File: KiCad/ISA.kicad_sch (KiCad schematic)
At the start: 4 parts

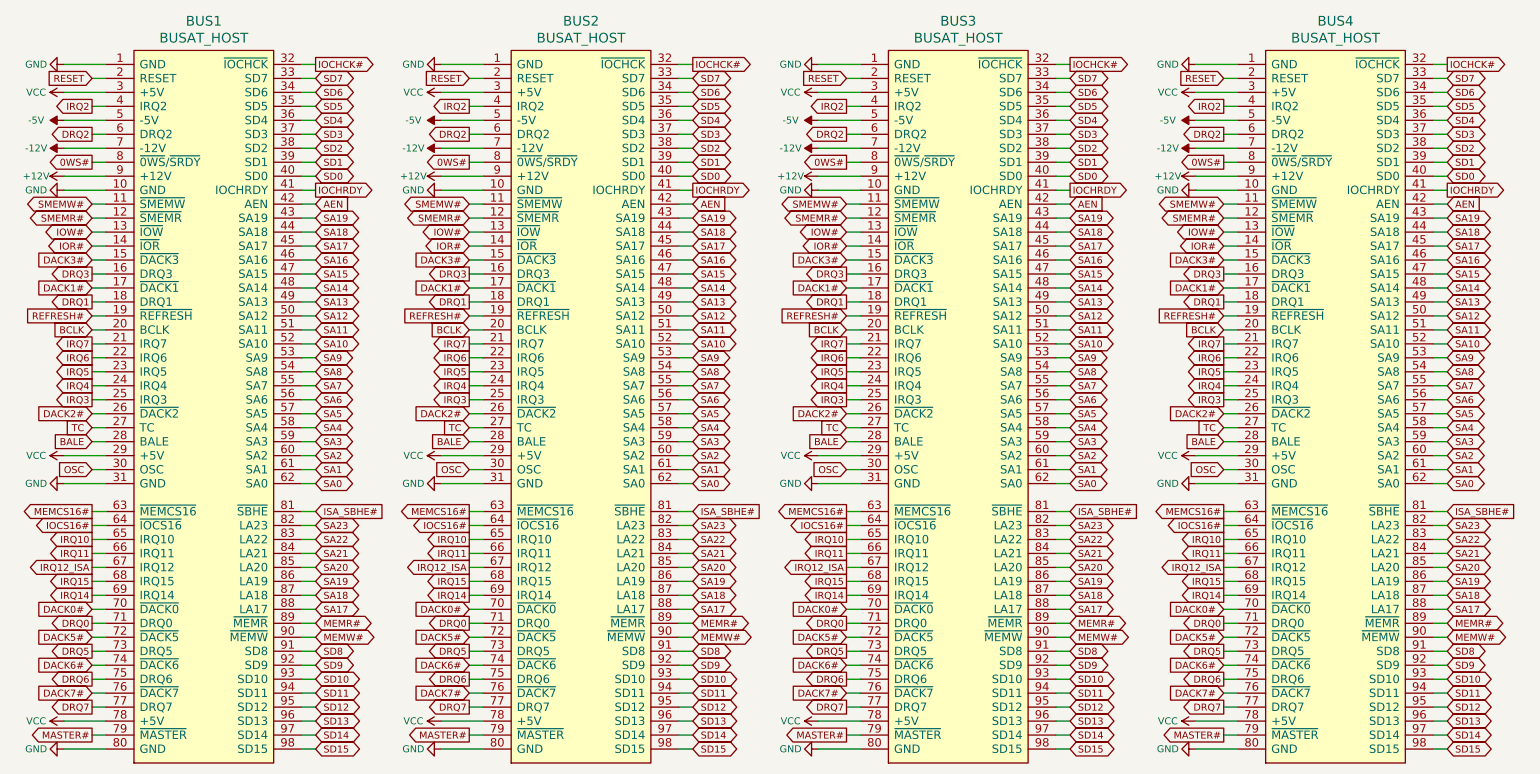
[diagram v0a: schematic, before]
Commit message: Version 0.3: Update DRAM schematic, pull-ups/pull-downs, CPU configuration jumpers
Signed-off-by: Sergey Kiselev <skiselev@gmail.com>
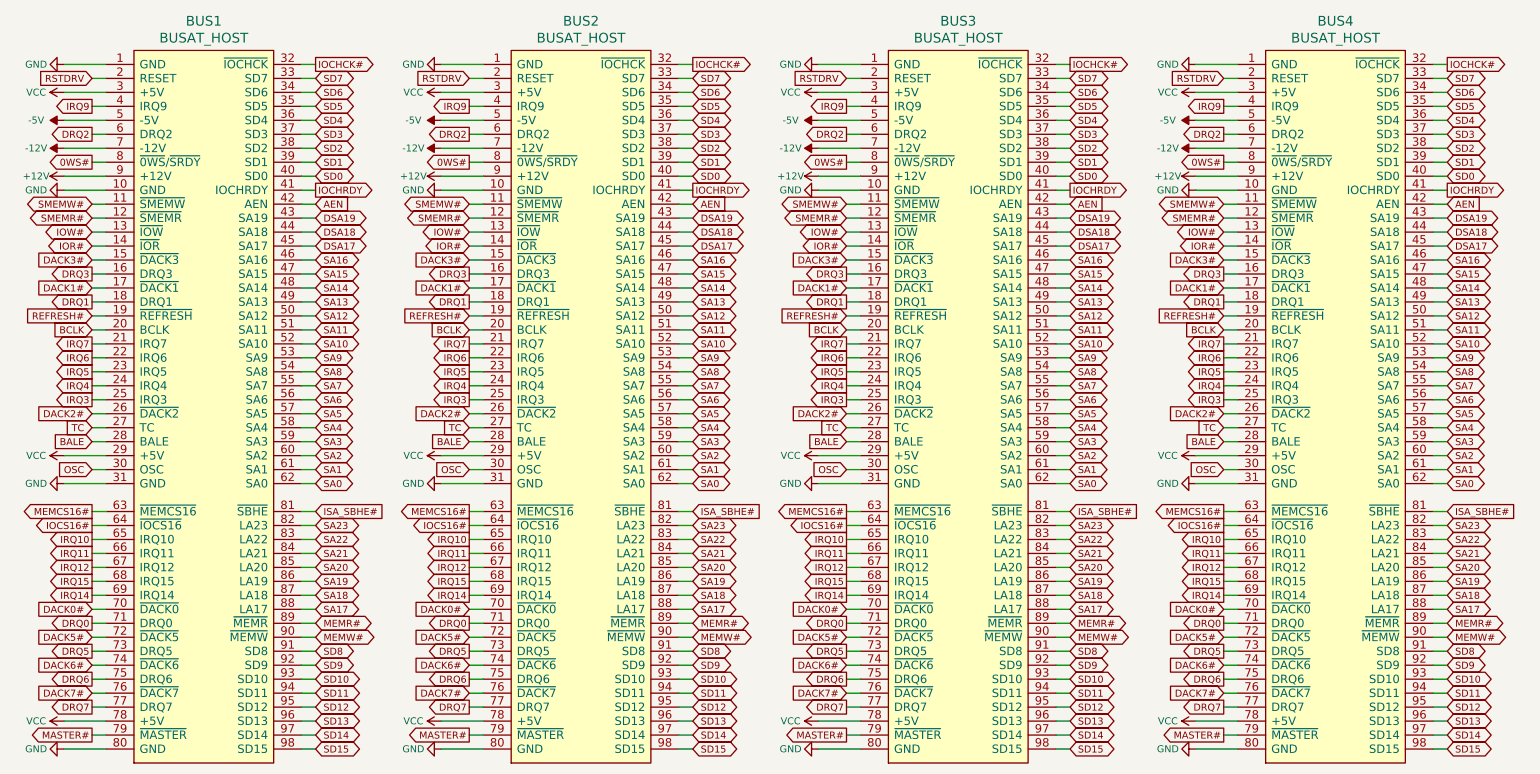
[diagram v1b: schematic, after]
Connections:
- net SA17: no longer BUS1.45 (SA17), BUS2.45 (SA17), BUS3.45 (SA17), BUS4.45 (SA17)
- net SA18: no longer BUS1.44 (SA18), BUS2.44 (SA18), BUS3.44 (SA18), BUS4.44 (SA18)
- net SA19: no longer BUS1.43 (SA19), BUS2.43 (SA19), BUS3.43 (SA19), BUS4.43 (SA19)
- net IRQ12_ISA renamed IRQ12
- net IRQ2 renamed IRQ9
- net RESET renamed RSTDRV
- new net DSA17: BUS1.45 (SA17), BUS2.45 (SA17), BUS3.45 (SA17), BUS4.45 (SA17)
- new net DSA18: BUS1.44 (SA18), BUS2.44 (SA18), BUS3.44 (SA18), BUS4.44 (SA18)
- new net DSA19: BUS1.43 (SA19), BUS2.43 (SA19), BUS3.43 (SA19), BUS4.43 (SA19)

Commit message: Version 0.4: Update chipset connection
Signed-off-by: Sergey Kiselev <skiselev@gmail.com>
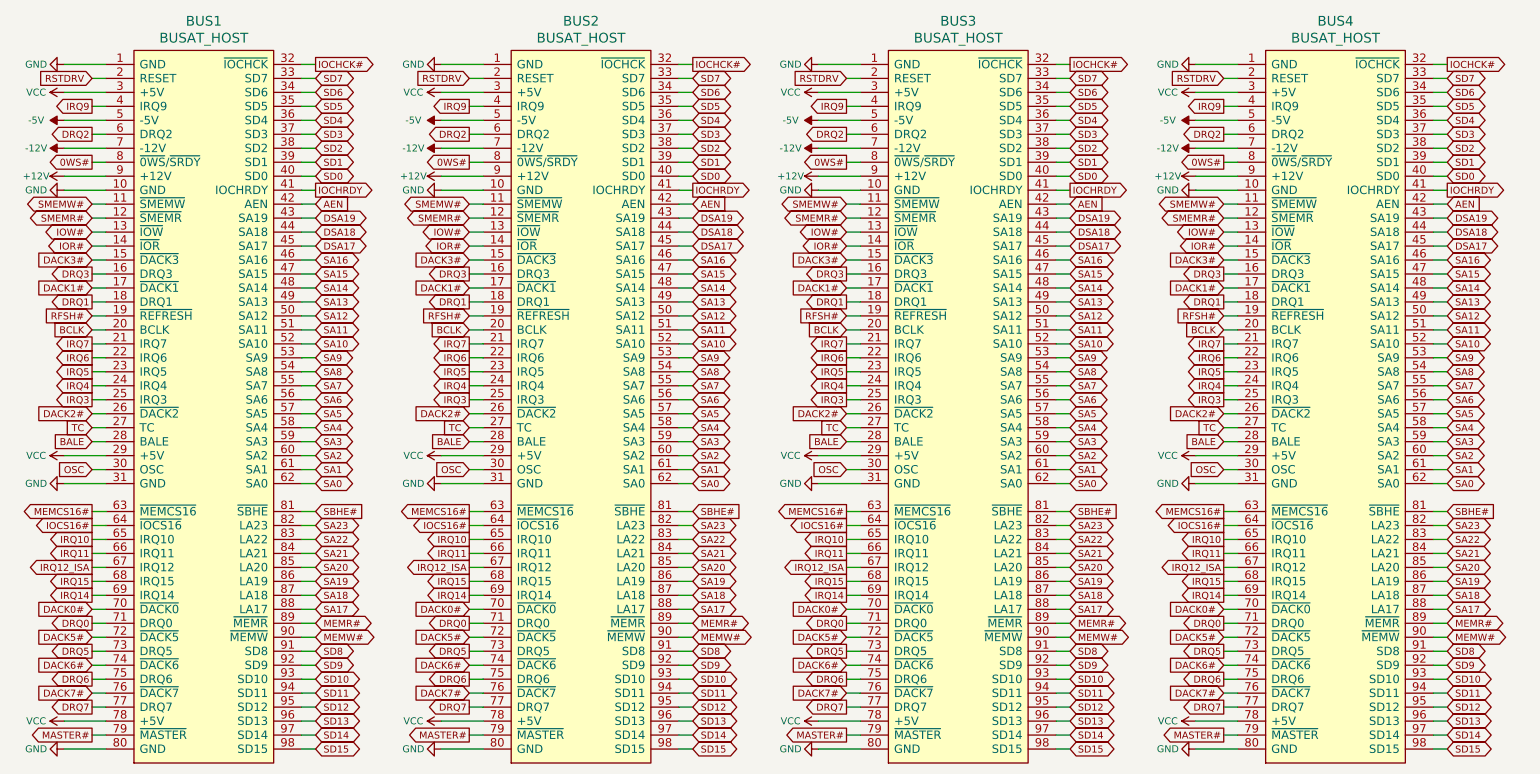
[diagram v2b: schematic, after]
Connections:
- net IRQ12 renamed IRQ12_ISA
- net ISA_SBHE# renamed SBHE#
- net REFRESH# renamed RFSH#
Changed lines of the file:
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@@
     )
   )
-  (global_label "IRQ12" (shape output) (at 231.14 116.84 180) (fields_autoplaced)
-    (effects (font (size 1.27 1.27)) (justify right))
-    (property "Intersheet References" "${INTERSHEET_REFS}" (id 0) (at 223.1915 116.7606 0)
+  (global_label "IRQ12_ISA" (shape output) (at 231.14 116.84 180) (fields_autoplaced)
+    (effects (font (size 1.27 1.27)) (justify right))
+    (property "Intersheet References" "${INTERSHEET_REFS}" (id 0) (at 219.321 116.7606 0)
       (effects (font (size 1.27 1.27)) (justify right) hide)
     )
@@
     )
   )
-  (global_label "ISA_SBHE#" (shape input) (at 203.2 106.68 0) (fields_autoplaced)
-    (effects (font (size 1.27 1.27)) (justify left))
-    (property "Intersheet References" "${INTERSHEET_REFS}" (id 0) (at 0 0 0)
-      (effects (font (size 1.27 1.27)) hide)
+  (global_label "SBHE#" (shape input) (at 203.2 106.68 0) (fields_autoplaced)
+    (effects (font (size 1.27 1.27)) (justify left))
+    (property "Intersheet References" "${INTERSHEET_REFS}" (id 0) (at 211.7532 106.6006 0)
+      (effects (font (size 1.27 1.27)) (justify left) hide)
     )
   )
@@
     )
   )
-  (global_label "IRQ12" (shape output) (at 162.56 116.84 180) (fields_autoplaced)
-    (effects (font (size 1.27 1.27)) (justify right))
-    (property "Intersheet References" "${INTERSHEET_REFS}" (id 0) (at 154.6115 116.7606 0)
+  (global_label "IRQ12_ISA" (shape output) (at 162.56 116.84 180) (fields_autoplaced)
+    (effects (font (size 1.27 1.27)) (justify right))
+    (property "Intersheet References" "${INTERSHEET_REFS}" (id 0) (at 150.741 116.7606 0)
       (effects (font (size 1.27 1.27)) (justify right) hide)
     )
@@
     )
   )
-  (global_label "IRQ12" (shape output) (at 25.4 116.84 180) (fields_autoplaced)
-    (effects (font (size 1.27 1.27)) (justify right))
-    (property "Intersheet References" "${INTERSHEET_REFS}" (id 0) (at 17.4515 116.7606 0)
+  (global_label "IRQ12_ISA" (shape output) (at 25.4 116.84 180) (fields_autoplaced)
+    (effects (font (size 1.27 1.27)) (justify right))
+    (property "Intersheet References" "${INTERSHEET_REFS}" (id 0) (at 13.581 116.7606 0)
       (effects (font (size 1.27 1.27)) (justify right) hide)
     )
@@
     )
   )
-  (global_label "ISA_SBHE#" (shape input) (at 271.78 106.68 0) (fields_autoplaced)
-    (effects (font (size 1.27 1.27)) (justify left))
-    (property "Intersheet References" "${INTERSHEET_REFS}" (id 0) (at 0 0 0)
-      (effects (font (size 1.27 1.27)) hide)
+  (global_label "SBHE#" (shape input) (at 271.78 106.68 0) (fields_autoplaced)
+    (effects (font (size 1.27 1.27)) (justify left))
+    (property "Intersheet References" "${INTERSHEET_REFS}" (id 0) (at 280.3332 106.6006 0)
+      (effects (font (size 1.27 1.27)) (justify left) hide)
     )
   )
@@
     )
   )
-  (global_label "IRQ12" (shape output) (at 93.98 116.84 180) (fields_autoplaced)
-    (effects (font (size 1.27 1.27)) (justify right))
-    (property "Intersheet References" "${INTERSHEET_REFS}" (id 0) (at 86.0315 116.7606 0)
+  (global_label "IRQ12_ISA" (shape output) (at 93.98 116.84 180) (fields_autoplaced)
+    (effects (font (size 1.27 1.27)) (justify right))
+    (property "Intersheet References" "${INTERSHEET_REFS}" (id 0) (at 82.161 116.7606 0)
       (effects (font (size 1.27 1.27)) (justify right) hide)
     )
@@
     )
   )
-  (global_label "REFRESH#" (shape input) (at 93.98 71.12 180) (fields_autoplaced)
-    (effects (font (size 1.27 1.27)) (justify right))
-    (property "Intersheet References" "${INTERSHEET_REFS}" (id 0) (at 0 0 0)
-      (effects (font (size 1.27 1.27)) hide)
+  (global_label "RFSH#" (shape input) (at 93.98 71.12 180) (fields_autoplaced)
+    (effects (font (size 1.27 1.27)) (justify right))
+    (property "Intersheet References" "${INTERSHEET_REFS}" (id 0) (at 85.4872 71.0406 0)
+      (effects (font (size 1.27 1.27)) (justify right) hide)
     )
   )
@@
     )
   )
-  (global_label "ISA_SBHE#" (shape input) (at 66.04 106.68 0) (fields_autoplaced)
-    (effects (font (size 1.27 1.27)) (justify left))
-    (property "Intersheet References" "${INTERSHEET_REFS}" (id 0) (at 0 0 0)
-      (effects (font (size 1.27 1.27)) hide)
+  (global_label "SBHE#" (shape input) (at 66.04 106.68 0) (fields_autoplaced)
+    (effects (font (size 1.27 1.27)) (justify left))
+    (property "Intersheet References" "${INTERSHEET_REFS}" (id 0) (at 74.5932 106.6006 0)
+      (effects (font (size 1.27 1.27)) (justify left) hide)
     )
   )
@@
     )
   )
-  (global_label "REFRESH#" (shape input) (at 231.14 71.12 180) (fields_autoplaced)
-    (effects (font (size 1.27 1.27)) (justify right))
-    (property "Intersheet References" "${INTERSHEET_REFS}" (id 0) (at 0 0 0)
-      (effects (font (size 1.27 1.27)) hide)
+  (global_label "RFSH#" (shape input) (at 231.14 71.12 180) (fields_autoplaced)
+    (effects (font (size 1.27 1.27)) (justify right))
+    (property "Intersheet References" "${INTERSHEET_REFS}" (id 0) (at 222.6472 71.0406 0)
+      (effects (font (size 1.27 1.27)) (justify right) hide)
     )
   )
@@
     )
   )
-  (global_label "REFRESH#" (shape input) (at 162.56 71.12 180) (fields_autoplaced)
-    (effects (font (size 1.27 1.27)) (justify right))
-    (property "Intersheet References" "${INTERSHEET_REFS}" (id 0) (at 0 0 0)
-      (effects (font (size 1.27 1.27)) hide)
+  (global_label "RFSH#" (shape input) (at 162.56 71.12 180) (fields_autoplaced)
+    (effects (font (size 1.27 1.27)) (justify right))
+    (property "Intersheet References" "${INTERSHEET_REFS}" (id 0) (at 154.0672 71.0406 0)
+      (effects (font (size 1.27 1.27)) (justify right) hide)
     )
   )
@@
     )
   )
-  (global_label "ISA_SBHE#" (shape input) (at 134.62 106.68 0) (fields_autoplaced)
-    (effects (font (size 1.27 1.27)) (justify left))
-    (property "Intersheet References" "${INTERSHEET_REFS}" (id 0) (at 0 0 0)
-      (effects (font (size 1.27 1.27)) hide)
+  (global_label "SBHE#" (shape input) (at 134.62 106.68 0) (fields_autoplaced)
+    (effects (font (size 1.27 1.27)) (justify left))
+    (property "Intersheet References" "${INTERSHEET_REFS}" (id 0) (at 143.1732 106.6006 0)
+      (effects (font (size 1.27 1.27)) (justify left) hide)
     )
   )
@@
     )
   )
-  (global_label "REFRESH#" (shape input) (at 25.4 71.12 180) (fields_autoplaced)
-    (effects (font (size 1.27 1.27)) (justify right))
-    (property "Intersheet References" "${INTERSHEET_REFS}" (id 0) (at 0 0 0)
-      (effects (font (size 1.27 1.27)) hide)
+  (global_label "RFSH#" (shape input) (at 25.4 71.12 180) (fields_autoplaced)
+    (effects (font (size 1.27 1.27)) (justify right))
+    (property "Intersheet References" "${INTERSHEET_REFS}" (id 0) (at 16.9072 71.0406 0)
+      (effects (font (size 1.27 1.27)) (justify right) hide)
     )
   )
@@
     )
   )
-  (symbol (lib_name "BUSAT_HOST_3") (lib_id "my_components:BUSAT_HOST") (at 45.72 87.63 0) (unit 1)
+  (symbol (lib_id "my_components:BUSAT_HOST") (at 45.72 87.63 0) (unit 1)
     (in_bom yes) (on_board yes)
     (property "Reference" "BUS1" (id 0) (at 45.72 17.526 0)
@@
     (pin "1")
   )
-  (symbol (lib_name "BUSAT_HOST_1") (lib_id "my_components:BUSAT_HOST") (at 114.3 87.63 0) (unit 1)
+  (symbol (lib_id "my_components:BUSAT_HOST") (at 114.3 87.63 0) (unit 1)
     (in_bom yes) (on_board yes)
     (property "Reference" "BUS2" (id 0) (at 114.3 17.526 0)
@@
     (pin "1")
   )
-  (symbol (lib_name "BUSAT_HOST_2") (lib_id "my_components:BUSAT_HOST") (at 182.88 87.63 0) (unit 1)
+  (symbol (lib_id "my_components:BUSAT_HOST") (at 182.88 87.63 0) (unit 1)
     (in_bom yes) (on_board yes)
     (property "Reference" "BUS3" (id 0) (at 182.88 17.526 0)
